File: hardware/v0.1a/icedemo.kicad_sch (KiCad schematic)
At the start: 54 parts, among them J1 SNES, J2 HDMI_A, SW1 TACT, U1 74LVC2T45, U2 74LVC2T45, U3 74LVC2T45, U4 SII902xA-mod, U5 TLV62568DBV

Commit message: First routing pass.
State after Electronics Let's Play stream.
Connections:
- net CSCL: now also A1.15 (P13); no longer A1.8 (P6)
- net CSDA: now also A1.16 (P14); no longer A1.7 (P5)
- net DE: now also A1.22 (P20); no longer A1.10 (P8)
- net GND: now also U4.73 (PAD); no longer U4.65 (PAD)
- net GPCLK: now also A1.21 (P19); no longer A1.2 (P0)
- net GPDAT0: now also A1.19 (P17); no longer A1.4 (P2)
- net GPDAT1: now also A1.18 (P16); no longer A1.5 (P3)
- net GPLATCH: now also A1.20 (P18); no longer A1.3 (P1)
- net GPSEL: now also A1.17 (P15); no longer A1.6 (P4)
- net HSYNC: now also A1.24 (P22); no longer A1.12 (P10)
- net IDCK: now also A1.10 (P8); no longer A1.13 (P11)
- net SPDIF: now also A1.25 (P23); no longer A1.9 (P7)
- net VD0: now also A1.2 (P0); no longer A1.14 (P12)
- net VD1: now also A1.3 (P1); no longer A1.15 (P13)
- net VD10: now also A1.13 (P11); no longer A1.24 (P22)
- net VD11: now also A1.14 (P12); no longer A1.25 (P23)
- net VD2: now also A1.4 (P2); no longer A1.16 (P14)
- net VD3: now also A1.5 (P3); no longer A1.17 (P15)
- net VD4: now also A1.6 (P4); no longer A1.18 (P16)
- net VD5: now also A1.7 (P5); no longer A1.19 (P17)
- net VD6: now also A1.8 (P6); no longer A1.20 (P18)
- net VD7: now also A1.9 (P7); no longer A1.21 (P19)
- net VD8: now also A1.11 (P9); no longer A1.22 (P20)
- net VD9: now also A1.12 (P10); no longer A1.23 (P21)
- net VSYNC: now also A1.23 (P21); no longer A1.11 (P9)
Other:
- note removed: "The exact pin assignment TBD"

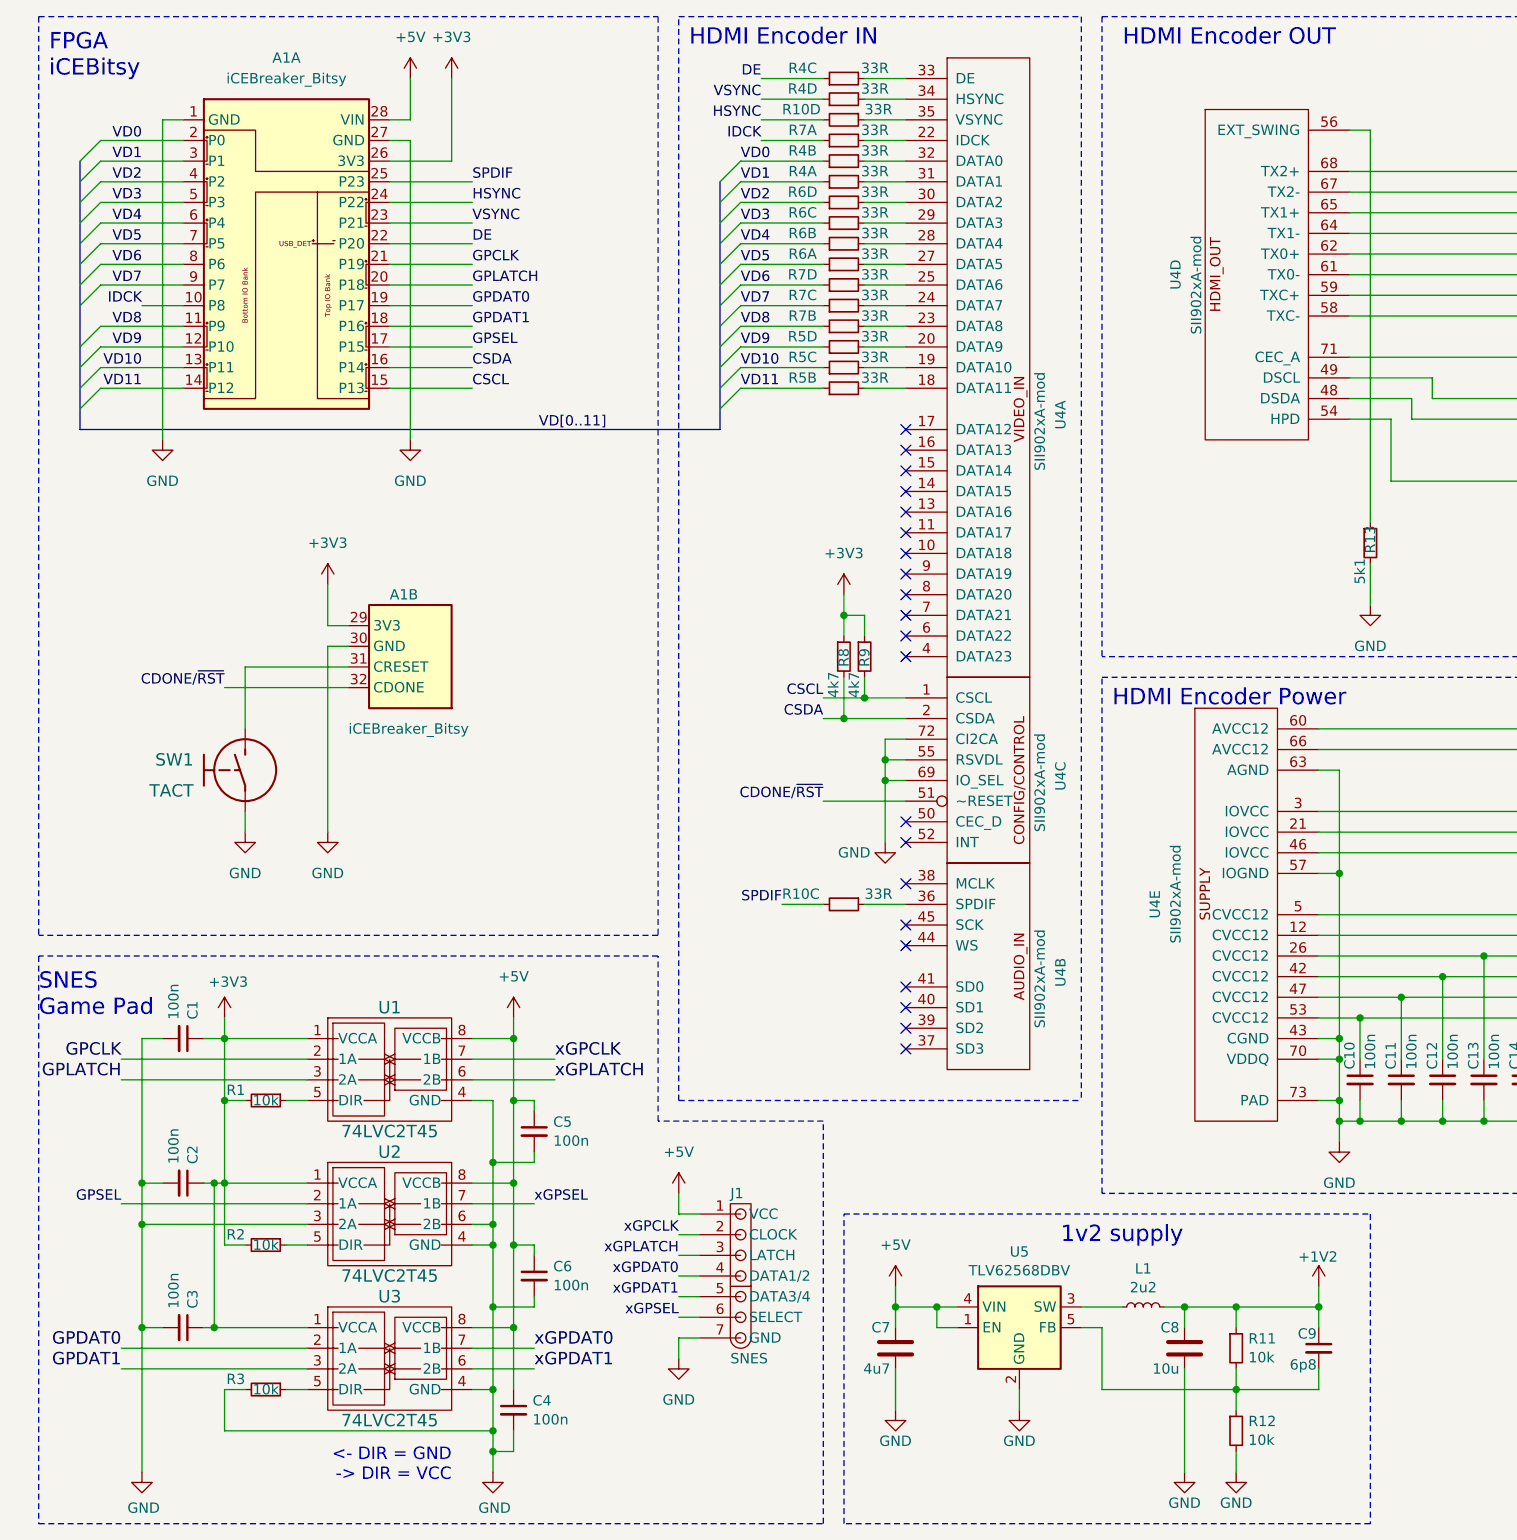
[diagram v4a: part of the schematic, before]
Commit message: Improved layout from Aug 10th stream.
Added GPIO expander and AUX connector.
Compressed board a bit.
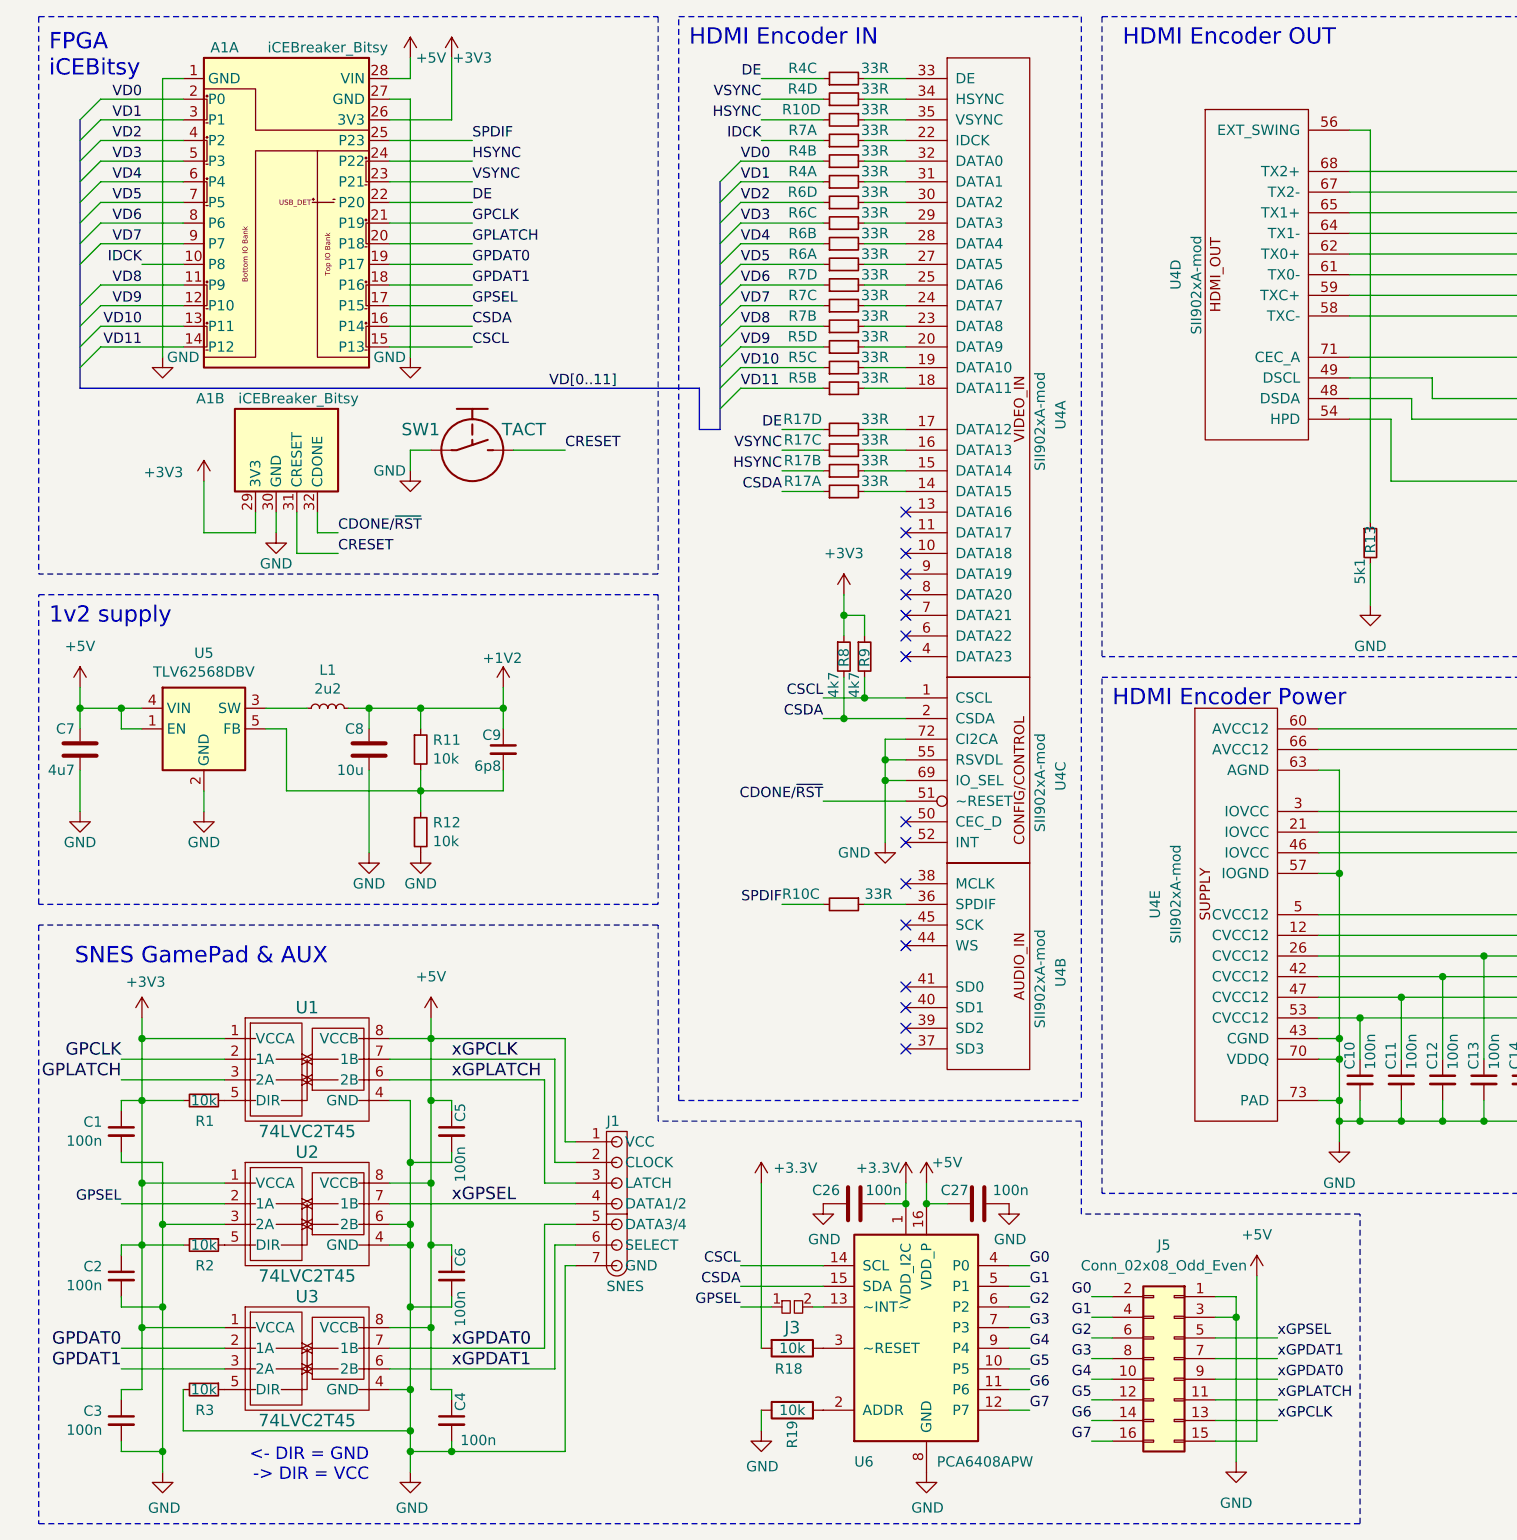
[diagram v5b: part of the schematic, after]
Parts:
- added C26, C27: 100n, Capacitor_SMD:C_0402_1005Metric, symbol Device:C
- added J3: pkl_jumper, pkl_jumpers:J_0603, symbol pkl_misc:pkl_jumper
- added J5: Conn_02x08_Odd_Even, Connector_PinHeader_2.54mm:PinHeader_2x08_P2.54mm_Horizontal, symbol Connector_Generic:Conn_02x08_Odd_Even
- added R17: 33R, pkl_dipol:R_Array_Convex_4x0402, symbol pkl_device:pkl_R4_Small
- added R18, R19: 10k, Resistor_SMD:R_0402_1005Metric, symbol Device:R
- added U6: PCA6408APW, Package_SO:TSSOP-16_4.4x5mm_P0.65mm, symbol Glasgow:PCA6408APW
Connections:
- net +3V3: now also C26.1, R18.2, U6.1 (VDD_I2C)
- net +5V: now also C27.1, J5.15 (Pin_15), U6.16 (VDD_P)
- net CSCL: now also U6.14 (SCL)
- net CSDA: now also R17.1, U6.15 (SDA)
- net DE: now also R17.7
- net GND: now also C26.2, C27.2, J5.1 (Pin_1), J5.3 (Pin_3), R19.1, U6.8 (GND)
- net GPSEL: now also J3.1
- net HSYNC: now also R17.3
- net VSYNC: now also R17.5
- net xGPCLK: now also J5.13 (Pin_13)
- net xGPDAT0: now also J1.5 (DATA3/4), J5.9 (Pin_9); no longer J1.4 (DATA1/2)
- net xGPDAT1: now also J1.6 (SELECT), J5.7 (Pin_7); no longer J1.5 (DATA3/4)
- net xGPLATCH: now also J5.11 (Pin_11)
- net xGPSEL: now also J1.4 (DATA1/2), J5.5 (Pin_5); no longer J1.6 (SELECT)
- net CRESET: now reaches A1.31 (CRESET), SW1.2
- net at U4.14 (DATA15): now also R17.2
- net at U4.15 (DATA14): now also R17.4
- net at U4.16 (DATA13): now also R17.6
- net at U4.17 (DATA12): now also R17.8
- new net: J3.2, U6.13 (~INT~)
- new net: R19.2, U6.2 (ADDR)
- new net: R18.1, U6.3 (~RESET)
- new net G0: J5.2 (Pin_2), U6.4 (P0)
- new net G1: J5.4 (Pin_4), U6.5 (P1)
- new net G2: J5.6 (Pin_6), U6.6 (P2)
- new net G3: J5.8 (Pin_8), U6.7 (P3)
- new net G4: J5.10 (Pin_10), U6.9 (P4)
- new net G5: J5.12 (Pin_12), U6.10 (P5)
- new net G6: J5.14 (Pin_14), U6.11 (P6)
- new net G7: J5.16 (Pin_16), U6.12 (P7)
- no-connect marks 22 -> 18
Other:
- note added: "SNES GamePad & AUX"
- note removed: "SNES Game Pad"
- title: icedemo -> iCECrash
- moved on the sheet: A1A, A1B, C1, C2, C3, C4, C5, C6, C7, C8, C9, J1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
